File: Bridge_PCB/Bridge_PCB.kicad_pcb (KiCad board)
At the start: 2 copper layers, 68.5 x 26.5 mm, 14 parts, among them P1 CONN_02X06, P10 CONN_02X04, P11 CONN_02X04, P12 CONN_02X08, P13 CONN_02X04, P14 CONN_02X04, P2 CONN_02X04, P3 CONN_02X04, P4 CONN_02X04, P5 CONN_02X04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

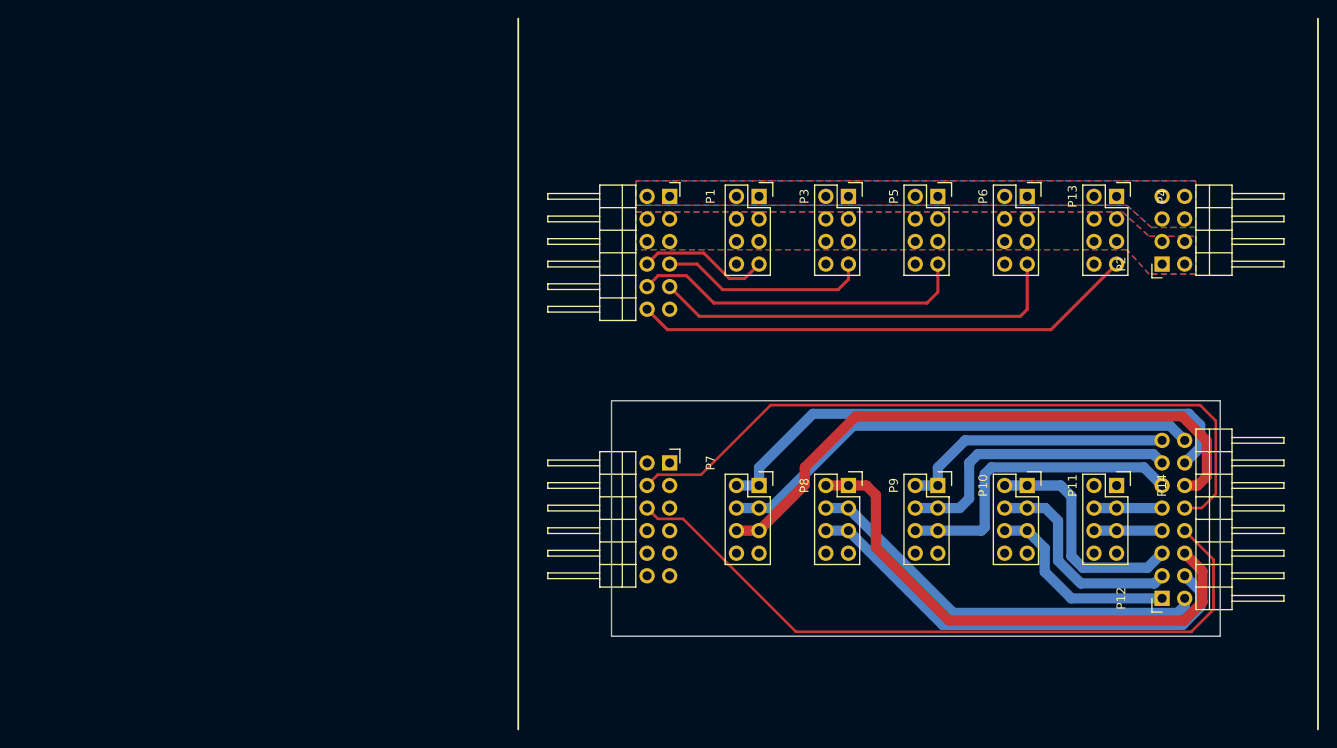
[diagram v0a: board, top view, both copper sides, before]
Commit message: Resize PCBs
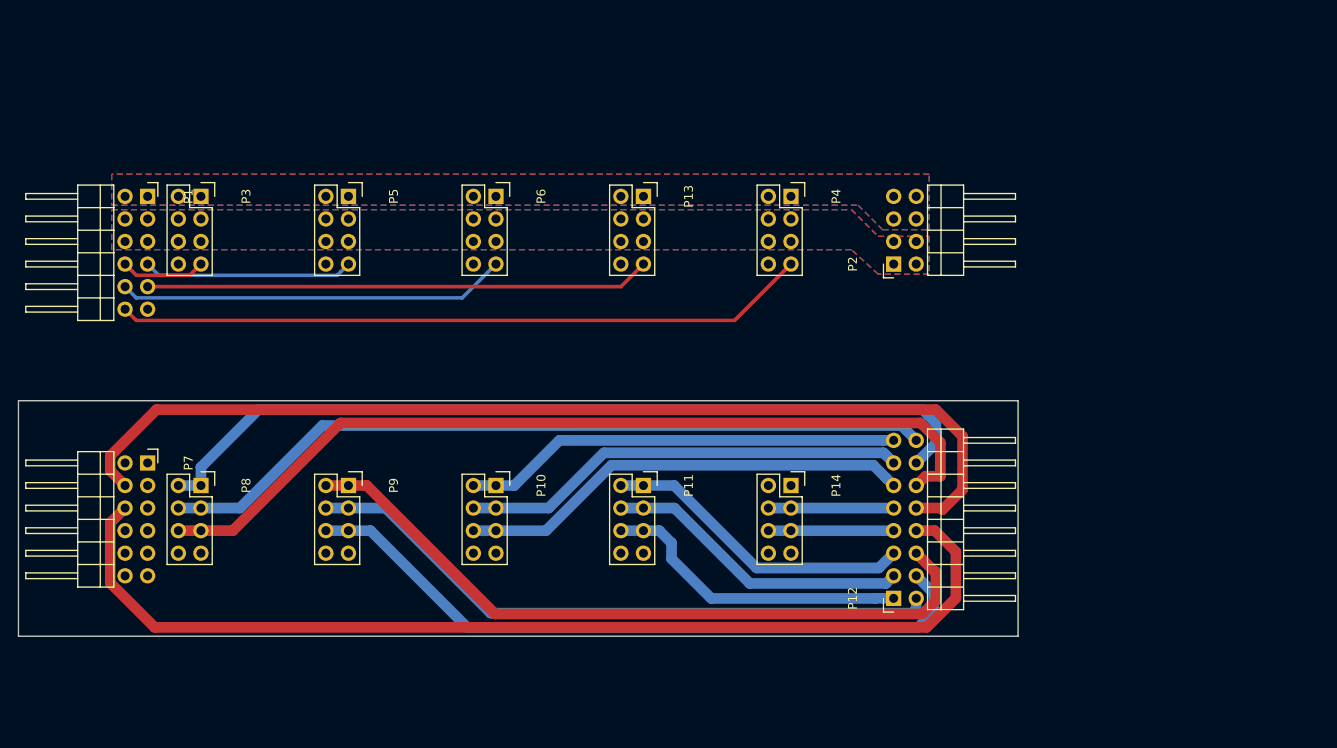
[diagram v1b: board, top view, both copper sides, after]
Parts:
- moved P3 62.8 mm to (64.3, 40.0)
- moved P8 62.8 mm to (64.3, 72.5)
- moved P1 58.8 mm to (58.3, 40.0)
- moved P7 58.8 mm to (58.3, 70.0)
- moved P5 56.3 mm to (80.9, 40.0)
- moved P9 56.3 mm to (80.9, 72.5)
- moved P10 49.7 mm to (97.5, 72.5)
- moved P6 49.7 mm to (97.5, 40.0)
- moved P11 43.2 mm to (114.1, 72.5)
- moved P13 43.2 mm to (114.1, 40.0)
- moved P14 36.7 mm to (130.7, 72.5)
- moved P4 36.7 mm to (130.7, 40.0)
- moved P12 30.2 mm to (142.2, 85.2)
- moved P2 30.2 mm to (142.2, 47.6)
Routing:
- net /SDA: track 80.8 -> 118.4 mm
- net /SCL: track 80.9 -> 115.6 mm
- net /A1: track 62.2 -> 96.0 mm
- net /A2: track 55.0 -> 87.6 mm
- net /A3: track 67.5 -> 98.6 mm
- net /B3: track 51.6 -> 78.5 mm
- net /B2: track 46.4 -> 72.7 mm
- net /B1: track 59.3 -> 81.6 mm
- net /CH_5: track 56.8 -> 78.1 mm
- net /C1: track 31.1 -> 49.4 mm
- net /C2: track 33.1 -> 50.3 mm
- net /C3: track 35.1 -> 51.3 mm
- net /D3: track 22.4 -> 34.9 mm
- net /D2: track 24.2 -> 34.6 mm
- net /CH_4: track 47.0 -> 56.9 mm
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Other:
- board size 68.5 x 26.5 mm -> 112.5 x 26.5 mm
- net class Default: trace_width 1.15 -> 1.2
